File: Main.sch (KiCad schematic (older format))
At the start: 70 parts, among them J6 Conn_01x03, J7 Conn_01x03, J8 Conn_01x06, Q1 CSD17307Q5A, Q2 CSD17307Q5A

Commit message: annotated schematic
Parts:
- U1: renamed from U?; value LM4120 -> LM4120AIM5-5.0; symbol CustomSymbols:LM4120 -> Main-rescue:LM4120-CustomSymbols
- U2: renamed from U?; symbol CustomSymbols:LTC2942 -> Main-rescue:LTC2942-CustomSymbols
- U3, U5: renamed from U?; symbol CustomSymbols:LM393 -> Main-rescue:LM393-CustomSymbols
- U4, U6: renamed from U?; symbol CustomSymbols:TPS2557 -> Main-rescue:TPS2557-CustomSymbols
- U7: renamed from U?; symbol CustomSymbols:SN74LVC2G08 -> Main-rescue:SN74LVC2G08-CustomSymbols
- gave numbers to parts that had none: 41
- renumbered AL/CC to AL/CC1, BAT+ to BAT+1, BAT- to BAT-1, CDR to CDR1, GND to GND1, MPB to MPB1, OUT to OUT1, PACK+ to PACK+1, SCL to SCL1, SDA to SDA1, SHORT to SHORT1

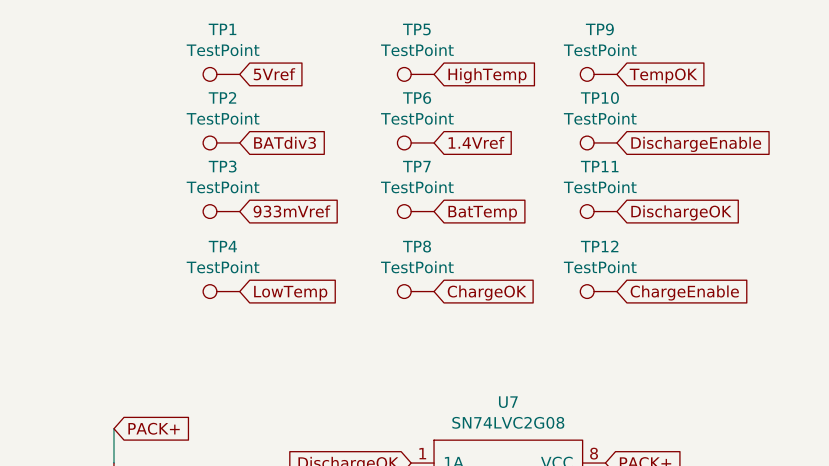
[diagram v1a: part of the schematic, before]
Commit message: Added footprints for symbols, need to find schottkys
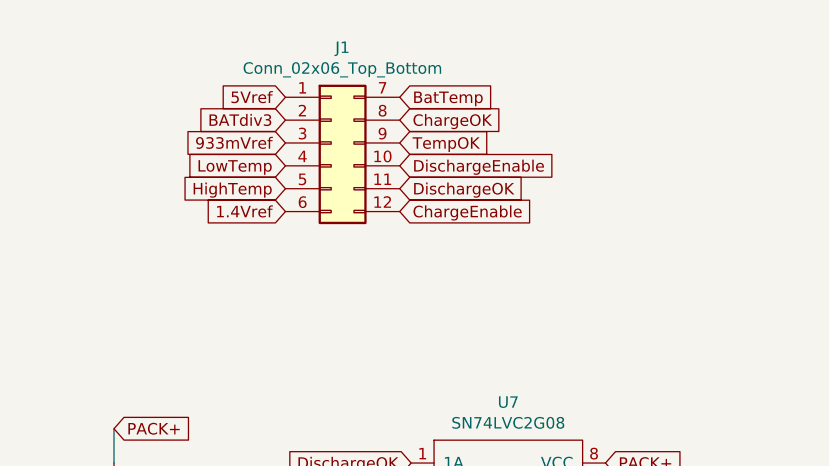
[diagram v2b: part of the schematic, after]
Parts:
- removed TP1, TP10, TP11, TP12, TP2, TP3, TP4, TP5, TP6, TP7, TP8, TP9: TestPoint, symbol Connector:TestPoint
- added J1: Conn_02x06_Top_Bottom, Connector_PinHeader_2.00mm:PinHeader_2x06_P2.00mm_Vertical, symbol Connector_Generic:Conn_02x06_Top_Bottom
- AL/CC1, BAT+1, BAT-1, PACK+1, SCL1, SDA1: footprint (none) -> Connector_PinHeader_2.00mm:PinHeader_1x01_P2.00mm_Vertical
- C1, C4, C5, C6, C7, C8: footprint (none) -> Capacitor_SMD:C_1206_3216Metric_Pad1.42x1.75mm_HandSolder
- C2, C3: footprint Capacitor_SMD:C_1206_3216Metric -> Capacitor_SMD:C_1206_3216Metric_Pad1.42x1.75mm_HandSolder
- R1, R10, R11, R12, R13, R14, R15, R17, R18, R19, R2, R20, R21, R22, R23, R6, R8, R9: footprint (none) -> Resistor_SMD:R_1206_3216Metric_Pad1.42x1.75mm_HandSolder
- R16, R3, R4, R5, R7: footprint Resistor_SMD:R_1206_3216Metric -> Resistor_SMD:R_1206_3216Metric_Pad1.42x1.75mm_HandSolder
- U1: footprint (none) -> Package_TO_SOT_SMD:SOT-23-5_HandSoldering
- U2: footprint (none) -> Package_DFN_QFN:DFN-6-1EP_3x2mm_P0.5mm_EP1.65x1.35mm
- U3, U5: footprint (none) -> Package_SO:SOIC-8-1EP_3.9x4.9mm_P1.27mm_EP2.29x3mm
- U7: footprint (none) -> Package_SO:SSOP-8_2.95x2.8mm_P0.65mm
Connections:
- net 1.4Vref: now also J1.6 (Pin_6)
- net 5Vref: now also J1.1 (Pin_1)
- net 933mVref: now also J1.3 (Pin_3)
- net BATdiv3: now also J1.2 (Pin_2)
- net BatTemp: now also J1.7 (Pin_7)
- net ChargeEnable: now also J1.12 (Pin_12)
- net ChargeOK: now also J1.8 (Pin_8)
- net DischargeEnable: now also J1.10 (Pin_10)
- net DischargeOK: now also J1.11 (Pin_11)
- net HighTemp: now also J1.5 (Pin_5)
- net LowTemp: now also J1.4 (Pin_4)
- net TempOK: now also J1.9 (Pin_9)

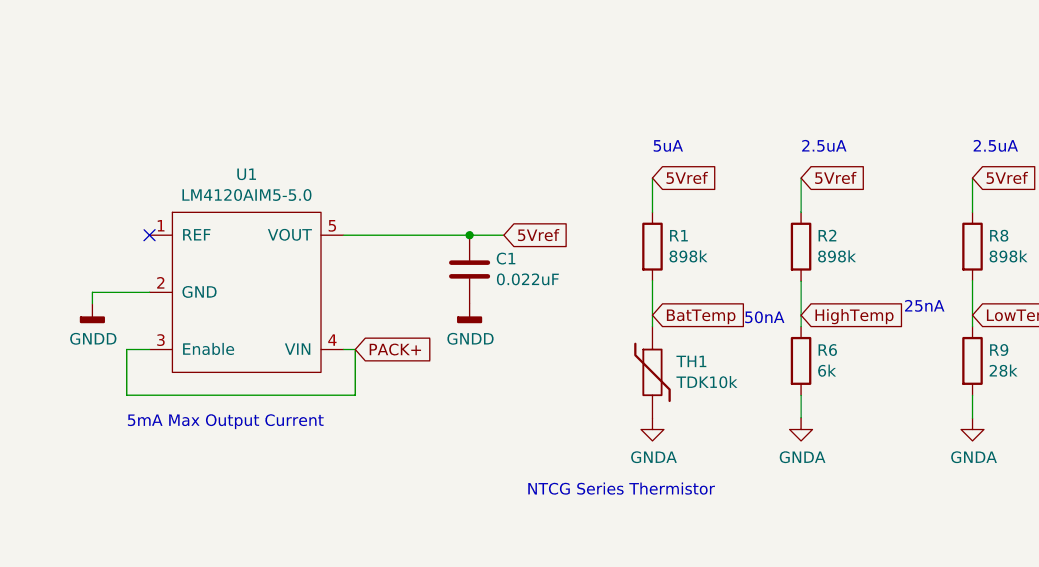
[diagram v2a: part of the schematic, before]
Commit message: changed_resistor
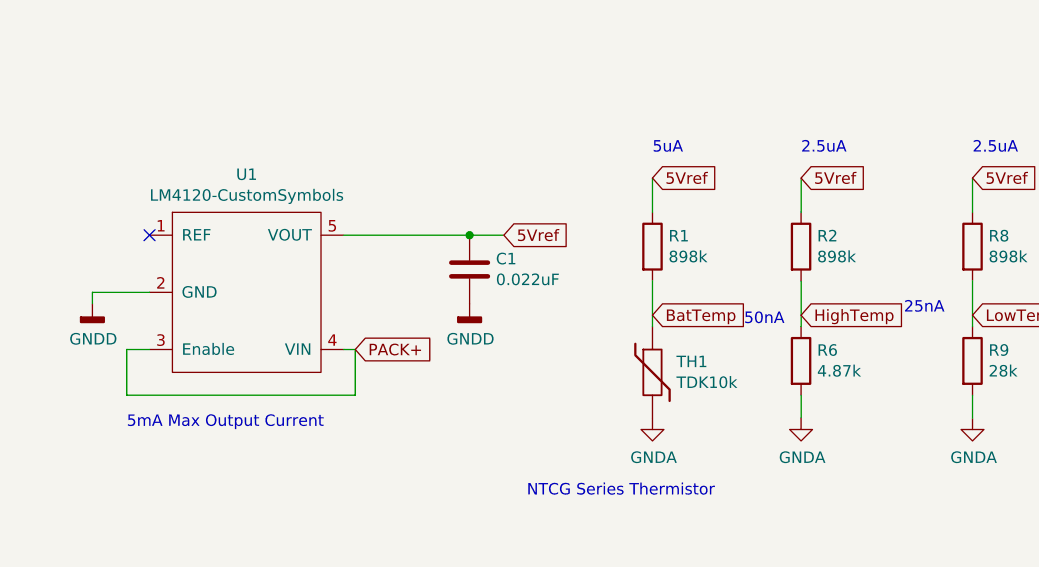
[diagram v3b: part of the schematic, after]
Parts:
- D1, D2: footprint (none) -> Diode_SMD:D_2114_3652Metric_Castellated
- R6: value 6k -> 4.87k
- TH1: footprint (none) -> Resistor_SMD:R_0402_1005Metric
- U1: value LM4120AIM5-5.0 -> LM4120-CustomSymbols
- U4, U6: footprint (none) -> tps2557:TPS2557
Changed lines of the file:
@@
 F 0 "U4" H 10625 8775 50  0000 C CNN
 F 1 "TPS2557" H 10625 8684 50  0000 C CNN
-F 2 "" H 10650 8650 50  0001 C CNN
+F 2 "tps2557:TPS2557" H 10650 8650 50  0001 C CNN
 F 3 "" H 10650 8650 50  0001 C CNN
 	1    10650 8350
@@
 F 0 "U6" H 12825 8775 50  0000 C CNN
 F 1 "TPS2557" H 12825 8684 50  0000 C CNN
-F 2 "" H 12850 8650 50  0001 C CNN
+F 2 "tps2557:TPS2557" H 12850 8650 50  0001 C CNN
 F 3 "" H 12850 8650 50  0001 C CNN
 	1    12850 8350
@@
 F 0 "D1" H 10600 7566 50  0000 C CNN
 F 1 "D_Schottky" H 10600 7475 50  0000 C CNN
-F 2 "" H 10600 7350 50  0001 C CNN
+F 2 "Diode_SMD:D_2114_3652Metric_Castellated" H 10600 7350 50  0001 C CNN
 F 3 "~" H 10600 7350 50  0001 C CNN
 	1    10600 7350
@@
 F 0 "D2" H 12850 7134 50  0000 C CNN
 F 1 "D_Schottky" H 12850 7225 50  0000 C CNN
-F 2 "" H 12850 7350 50  0001 C CNN
+F 2 "Diode_SMD:D_2114_3652Metric_Castellated" H 12850 7350 50  0001 C CNN
 F 3 "~" H 12850 7350 50  0001 C CNN
 	1    12850 7350
@@
 Wire Wire Line
 	1300 6150 1200 6150
-$Comp
-L Main-rescue:LM4120-CustomSymbols U1
-U 1 1 5E3E74B3
-P 1750 5900
-F 0 "U1" H 1725 6415 50  0000 C CNN
-F 1 "LM4120AIM5-5.0" H 1725 6324 50  0000 C CNN
-F 2 "Package_TO_SOT_SMD:SOT-23-5_HandSoldering" H 1750 5900 50  0001 C CNN
-F 3 "" H 1750 5900 50  0001 C CNN
-	1    1750 5900
-	1    0    0    -1
-$EndComp
 Text GLabel 4150 6000 2    50   Input ~ 0
 HighTemp
@@
 P 4150 6200
 F 0 "R6" H 4220 6246 50  0000 L CNN
-F 1 "6k" H 4220 6155 50  0000 L CNN
+F 1 "4.87k" H 4220 6155 50  0000 L CNN
 F 2 "Resistor_SMD:R_1206_3216Metric_Pad1.42x1.75mm_HandSolder" V 4080 6200 50  0001 C CNN
 F 3 "~" H 4150 6200 50  0001 C CNN
@@
 F 0 "TH1" H 3605 6296 50  0000 L CNN
 F 1 "TDK10k" H 3605 6205 50  0000 L CNN
-F 2 "" H 3500 6250 50  0001 C CNN
+F 2 "Resistor_SMD:R_0402_1005Metric" H 3500 6250 50  0001 C CNN
 F 3 "~" H 3500 6250 50  0001 C CNN
 	1    3500 6250
@@
 Text GLabel 13400 4350 0    50   Input ~ 0
 LowTemp
+$Comp
+L Main-rescue:LM4120-CustomSymbols U1
+U 1 1 5DEBDC7C
+P 1750 5900
+F 0 "U1" H 1725 6415 50  0000 C CNN
+F 1 "LM4120-CustomSymbols" H 1725 6324 50  0000 C CNN
+F 2 "Package_TO_SOT_SMD:SOT-23-5_HandSoldering" H 1750 5900 50  0001 C CNN
+F 3 "" H 1750 5900 50  0001 C CNN
+	1    1750 5900
+	1    0    0    -1
+$EndComp
 $EndSCHEMATC

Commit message: added txt
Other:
- note added: "Silk screen will be used to label all the TP's\n\n"
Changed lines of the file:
@@
 	1    0    0    -1
 $EndComp
+Text Notes 13100 3800 0    50   ~ 0
+Silk screen will be used to label all the TP's\n\n
 $EndSCHEMATC

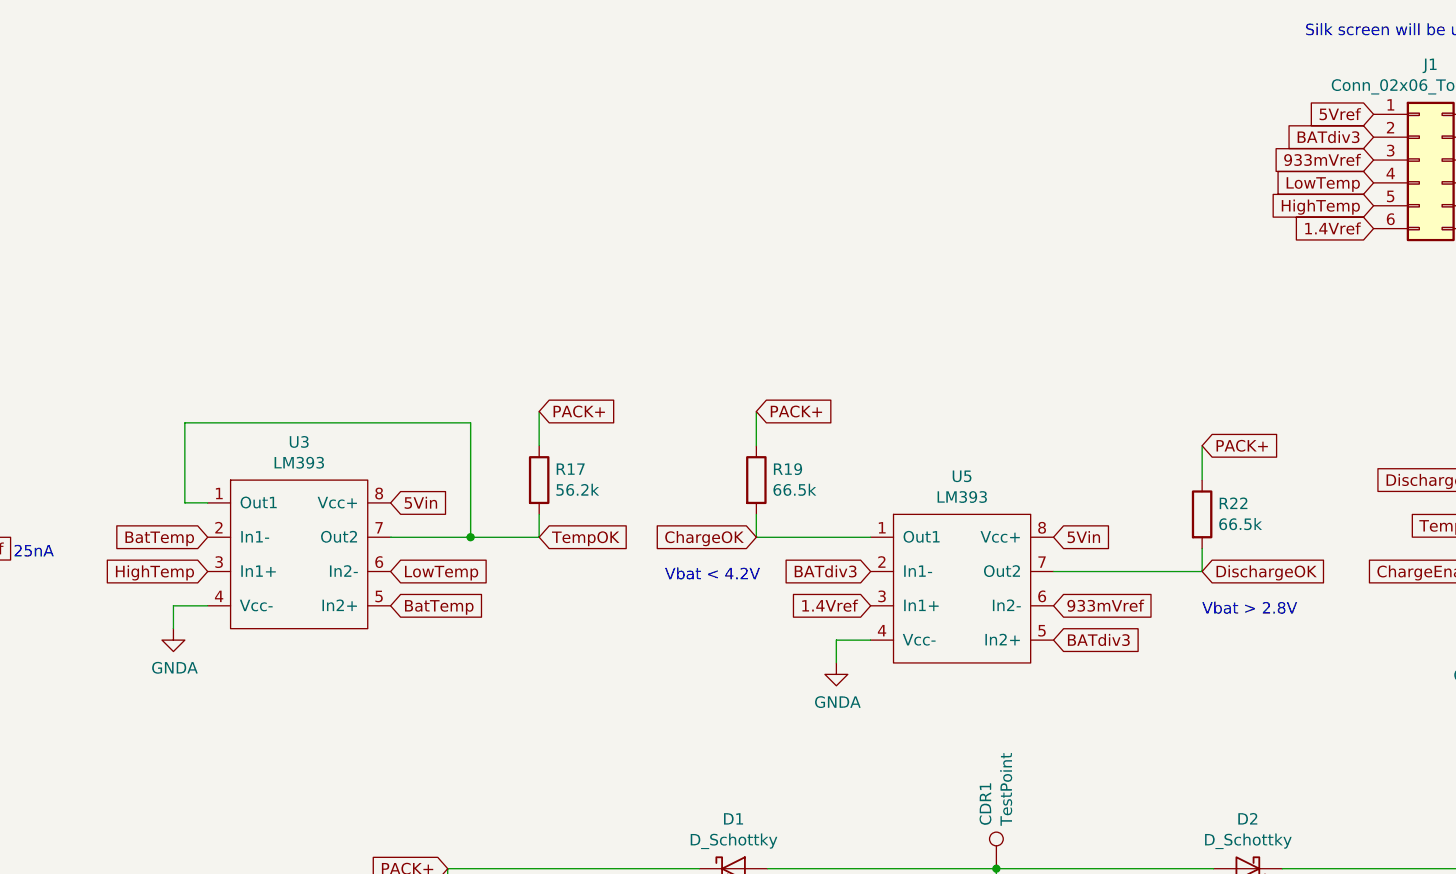
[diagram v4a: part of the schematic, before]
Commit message: Changed Comparator supply to Pack+. Changed pull-up resistor supply from Pack to 5Vref, changed values of pull-up resistors.
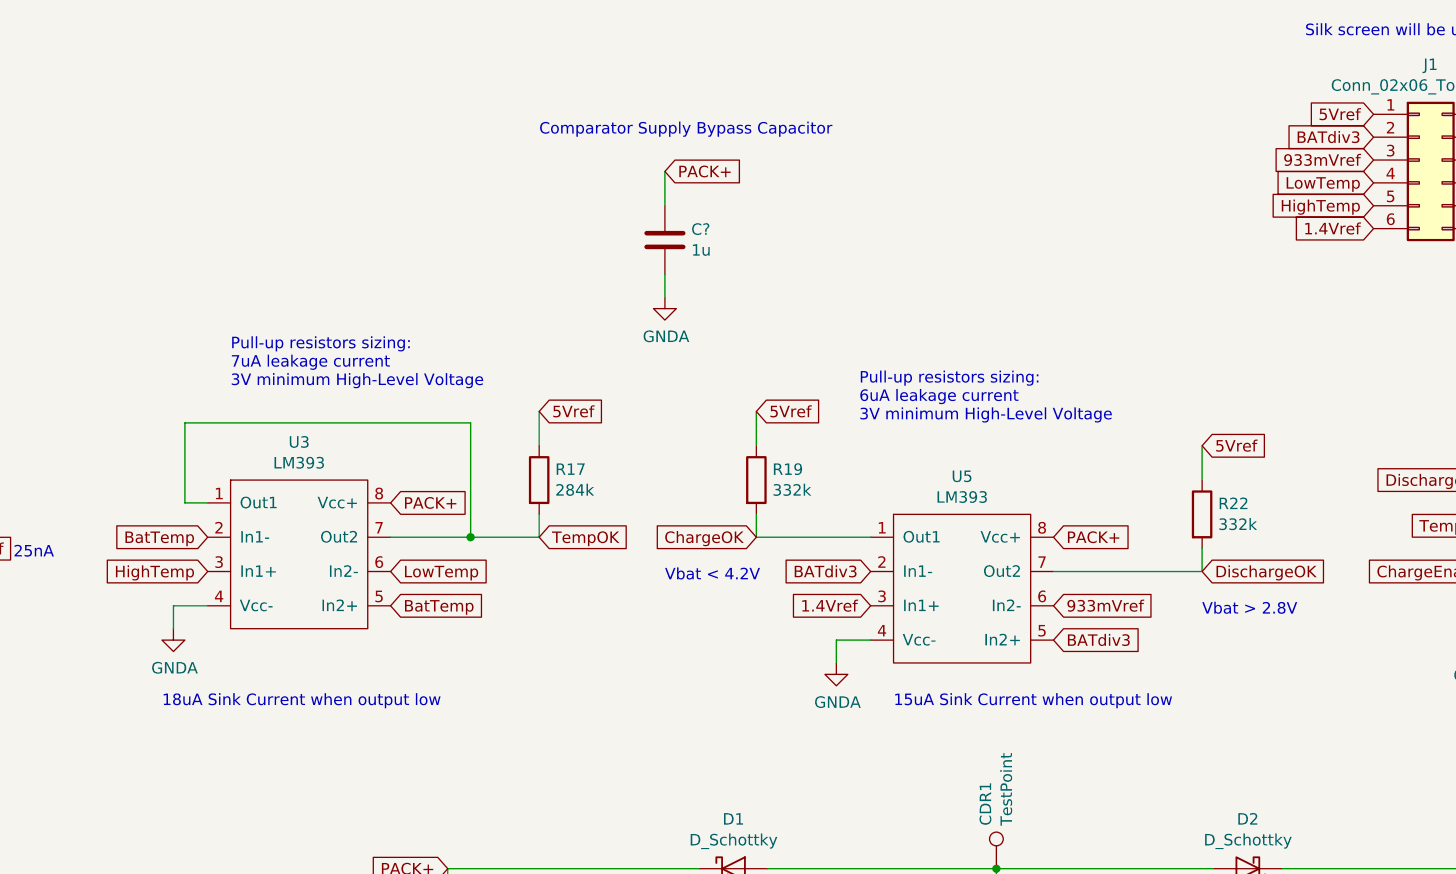
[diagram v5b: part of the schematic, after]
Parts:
- added C?: 1u, Capacitor_SMD:C_1206_3216Metric_Pad1.42x1.75mm_HandSolder, symbol Device:C
- R17: value 56.2k -> 284k
- R19, R22: value 66.5k -> 332k
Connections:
- net 5Vin is gone; now on net PACK+: U3.8 (Vcc+), U5.8 (Vcc+)
- net 5Vref: now also R17.1, R19.1, R22.1
- net GNDA: now also C?.2
- net PACK+: now also C?.1; no longer R17.1, R19.1, R22.1
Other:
- note added: "15uA Sink Current when output low"
- note added: "18uA Sink Current when output low"
- note added: "Comparator Supply Bypass Capacitor"
- note added: "Pull-up resistors sizing:\n6uA leakage current\n3V minimum High-Level Voltage"
- note added: "Pull-up resistors sizing:\n7uA leakage current\n3V minimum High-Level Voltage"
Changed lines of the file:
@@
 Text GLabel 14950 8350 2    50   Input ~ 0
 MPB
-Text GLabel 9750 5350 2    50   Input ~ 0
-PACK+
 Text GLabel 3500 5400 2    50   Input ~ 0
 5Vref
@@
 Wire Wire Line
 	8200 5400 9450 5400
-Text GLabel 10700 5350 2    50   Input ~ 0
-PACK+
 Text GLabel 10700 5900 0    50   Input ~ 0
 ChargeOK
@@
 P 10700 5650
 F 0 "R19" H 10770 5696 50  0000 L CNN
-F 1 "66.5k" H 10770 5605 50  0000 L CNN
+F 1 "332k" H 10770 5605 50  0000 L CNN
 F 2 "Resistor_SMD:R_1206_3216Metric_Pad1.42x1.75mm_HandSolder" V 10630 5650 50  0001 C CNN
 F 3 "~" H 10700 5650 50  0001 C CNN
@@
 Text GLabel 11200 6050 0    50   Input ~ 0
 BATdiv3
-Text GLabel 12650 5500 2    50   Input ~ 0
-PACK+
 Wire Wire Line
 	12650 5500 12650 5650
@@
 P 12650 5800
 F 0 "R22" H 12720 5846 50  0000 L CNN
-F 1 "66.5k" H 12720 5755 50  0000 L CNN
+F 1 "332k" H 12720 5755 50  0000 L CNN
 F 2 "Resistor_SMD:R_1206_3216Metric_Pad1.42x1.75mm_HandSolder" V 12580 5800 50  0001 C CNN
 F 3 "~" H 12650 5800 50  0001 C CNN
@@
 	1    0    0    -1
 $EndComp
-Text GLabel 12000 5900 2    50   Input ~ 0
-5Vin
 $Comp
 L Main-rescue:LM393-CustomSymbols U5
@@
 P 9750 5650
 F 0 "R17" H 9820 5696 50  0000 L CNN
-F 1 "56.2k" H 9820 5605 50  0000 L CNN
+F 1 "284k" H 9820 5605 50  0000 L CNN
 F 2 "Resistor_SMD:R_1206_3216Metric_Pad1.42x1.75mm_HandSolder" V 9680 5650 50  0001 C CNN
 F 3 "~" H 9750 5650 50  0001 C CNN
@@
 	1    0    0    -1
 $EndComp
-Text GLabel 9100 5750 2    50   Input ~ 0
-5Vin
 $Comp
 L Main-rescue:LM393-CustomSymbols U3
@@
 Text Notes 13100 3800 0    50   ~ 0
 Silk screen will be used to label all the TP's\n\n
+Text GLabel 12650 5500 2    50   Input ~ 0
+5Vref
+Text GLabel 10700 5350 2    50   Input ~ 0
+5Vref
+Text GLabel 9750 5350 2    50   Input ~ 0
+5Vref
+Text Notes 11150 5400 0    50   ~ 0
+Pull-up resistors sizing:\n6uA leakage current\n3V minimum High-Level Voltage
+Text Notes 8400 5250 0    50   ~ 0
+Pull-up resistors sizing:\n7uA leakage current\n3V minimum High-Level Voltage
+Text Notes 8100 6650 0    50   ~ 0
+18uA Sink Current when output low
+Text Notes 11300 6650 0    50   ~ 0
+15uA Sink Current when output low
+Text GLabel 12000 5900 2    50   Input ~ 0
+PACK+
+Text GLabel 9100 5750 2    50   Input ~ 0
+PACK+
+Text GLabel 10300 4300 2    50   Input ~ 0
+PACK+
+$Comp
+L Device:C C?
+U 1 1 5DEA295E
+P 10300 4600
+F 0 "C?" H 10415 4646 50  0000 L CNN
+F 1 "1u" H 10415 4555 50  0000 L CNN
+F 2 "Capacitor_SMD:C_1206_3216Metric_Pad1.42x1.75mm_HandSolder" H 10338 4450 50  0001 C CNN
+F 3 "~" H 10300 4600 50  0001 C CNN
+	1    10300 4600
+	1    0    0    -1
+$EndComp
+$Comp
+L power:GNDA #PWR?
+U 1 1 5DEA2F75
+P 10300 4850
+F 0 "#PWR?" H 10300 4600 50  0001 C CNN
+F 1 "GNDA" H 10305 4677 50  0000 C CNN
+F 2 "" H 10300 4850 50  0001 C CNN
+F 3 "" H 10300 4850 50  0001 C CNN
+	1    10300 4850
+	1    0    0    -1
+$EndComp
+Wire Wire Line
+	10300 4450 10300 4300
+Wire Wire Line
+	10300 4750 10300 4850
+Text Notes 9750 4150 0    50   ~ 0
+Comparator Supply Bypass Capacitor
 $EndSCHEMATC

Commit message: worked on pcb
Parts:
- gave numbers to parts that had none: 1
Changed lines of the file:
@@
 PACK+
 $Comp
-L Device:C C?
+L Device:C C9
 U 1 1 5DEA295E
 P 10300 4600
-F 0 "C?" H 10415 4646 50  0000 L CNN
+F 0 "C9" H 10415 4646 50  0000 L CNN
 F 1 "1u" H 10415 4555 50  0000 L CNN
 F 2 "Capacitor_SMD:C_1206_3216Metric_Pad1.42x1.75mm_HandSolder" H 10338 4450 50  0001 C CNN
@@
 $EndComp
 $Comp
-L power:GNDA #PWR?
+L power:GNDA #PWR0101
 U 1 1 5DEA2F75
 P 10300 4850
-F 0 "#PWR?" H 10300 4600 50  0001 C CNN
+F 0 "#PWR0101" H 10300 4600 50  0001 C CNN
 F 1 "GNDA" H 10305 4677 50  0000 C CNN
 F 2 "" H 10300 4850 50  0001 C CNN
